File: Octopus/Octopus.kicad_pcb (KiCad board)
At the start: 2 copper layers, 205.8 x 111.7 mm, 61 parts, among them J1 FM6725 MIDI IN, J10 RN112BPC, J11 Button panel, J12 FM6725 MIDI THRU, J2 9-12VDC IN, J3 RN112BPC, J4 RN112BPC, J5 RN112BPC, J6 RN112BPC, J7 RN112BPC, J8 RN112BPC, J9 RN112BPC, K1 G5V-1, K10 G5V-1, K11 G5V-1, K12 G5V-1, K13 G5V-1, K14 G5V-1, K15 G5V-1, K16 G5V-1, K2 G5V-1, K3 G5V-1, K4 G5V-1, K5 G5V-1, K6 G5V-1, K7 G5V-1, K8 G5V-1, K9 G5V-1, U1 Teensy4.1, U2 6N138, U3 ULN2803A, U4 R-78E5.0-1.0, U5 ULN2803A, U6 74HCT14

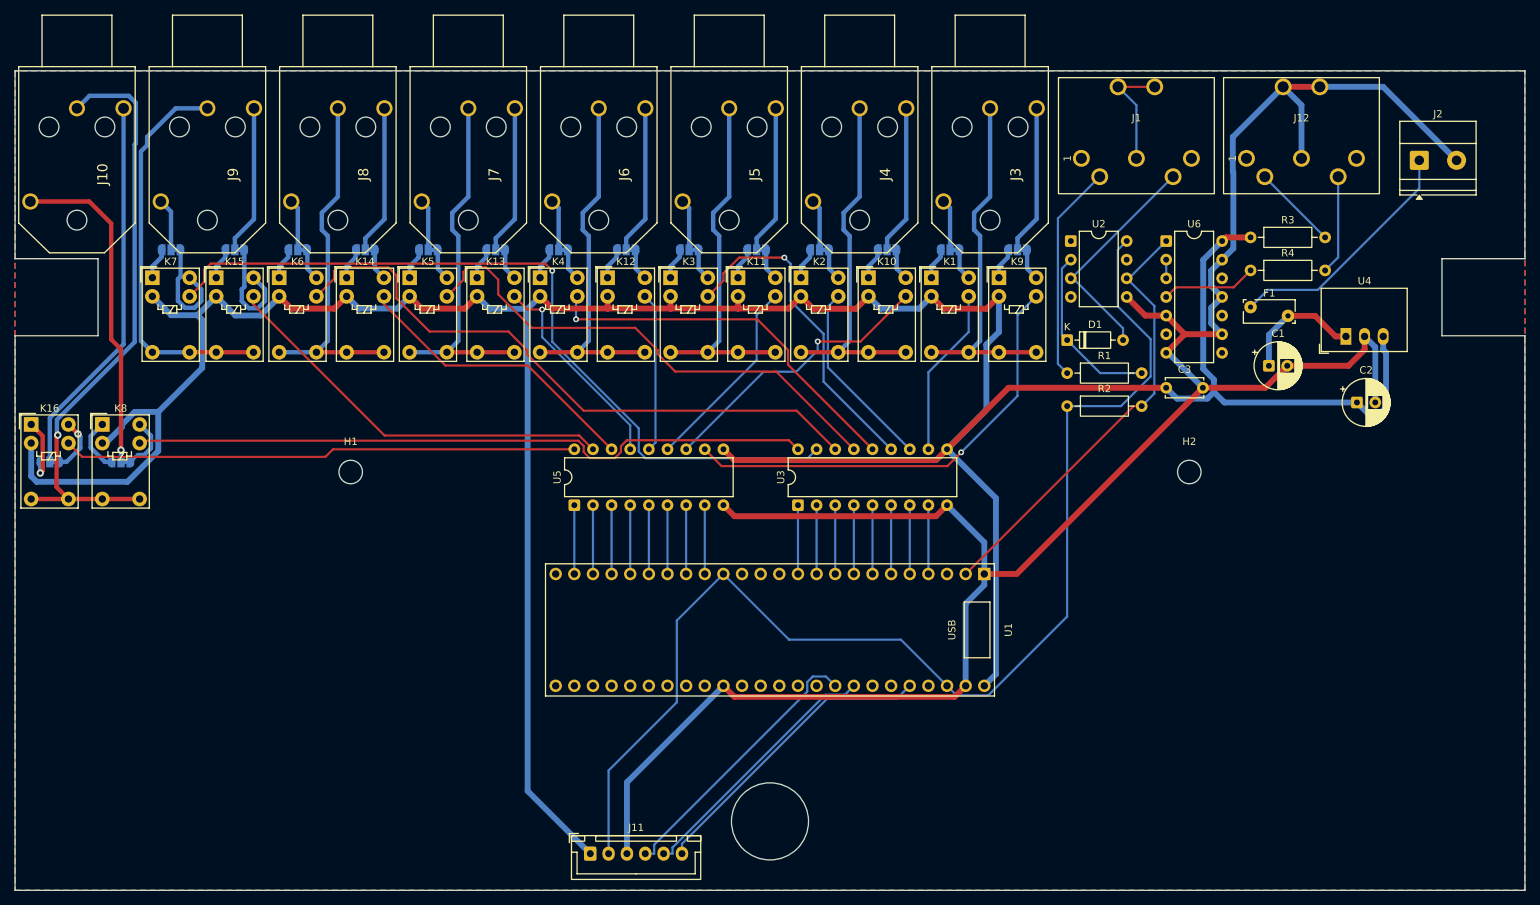
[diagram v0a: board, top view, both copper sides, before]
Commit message: Added standard power supply
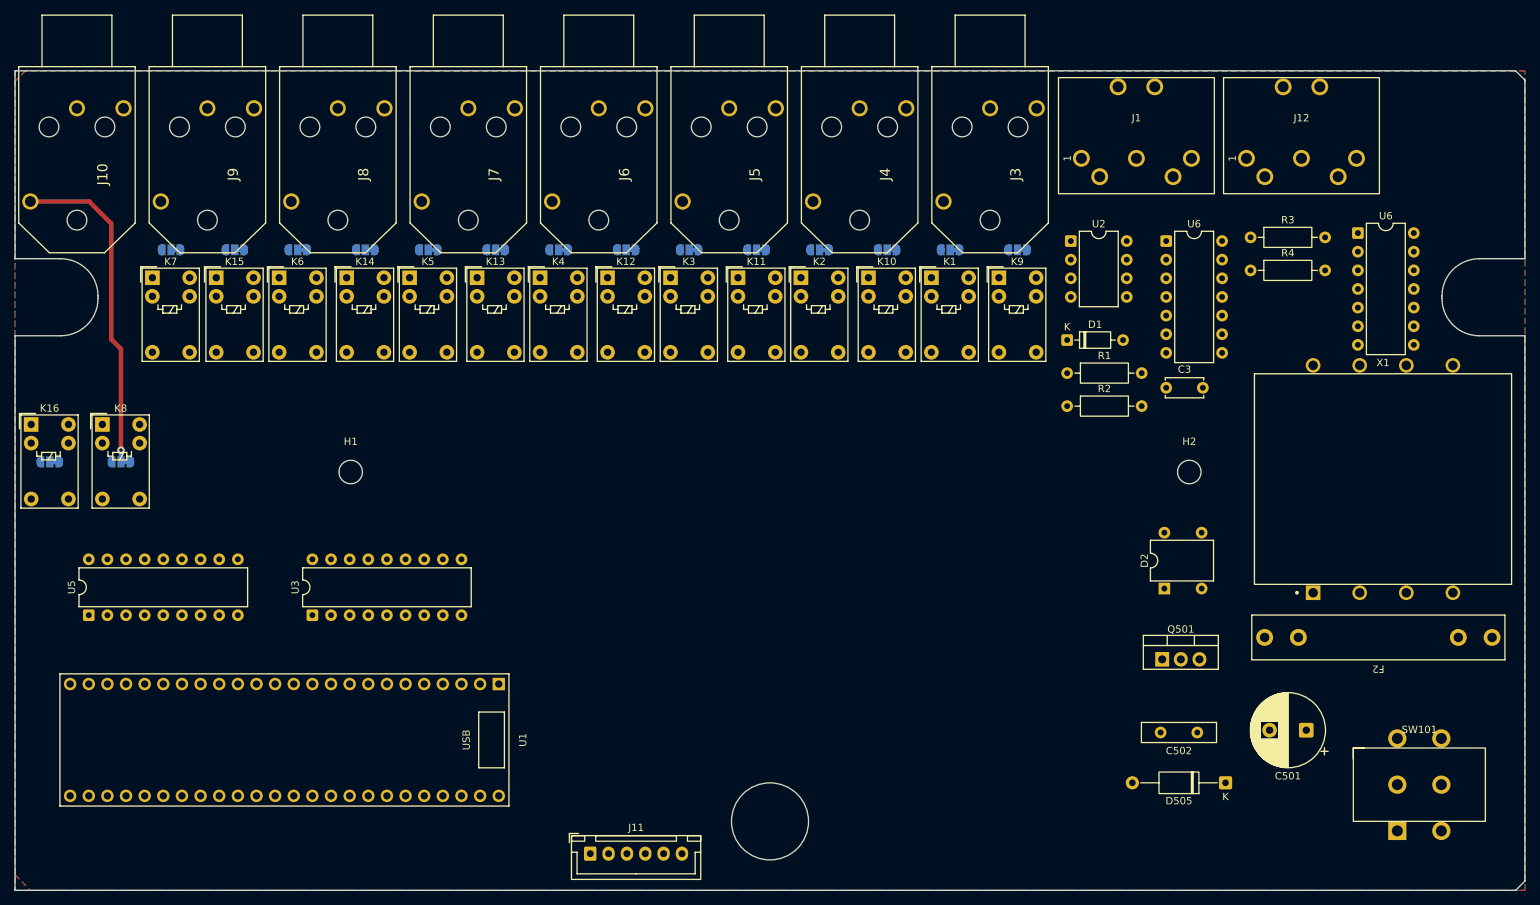
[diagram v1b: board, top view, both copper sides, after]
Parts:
- removed C1: 10uF 25V, Capacitor_THT:CP_Radial_D6.3mm_P2.50mm
- removed C2: 22uF 16V, Capacitor_THT:CP_Radial_D6.3mm_P2.50mm
- removed F1: MF-RHT070 0.7A, Fuse:Fuse_Bourns_MF-RHT070
- removed J2: 9-12VDC IN, TerminalBlock_Phoenix:TerminalBlock_Phoenix_MKDS-1,5-2-5.08_1x02_P5.08mm_Horizontal
- removed U4: R-78E5.0-1.0, Converter_DCDC:Converter_DCDC_RECOM_R-78E-0.5_THT
- added C501: 1000u, Capacitor_THT:CP_Radial_D10.0mm_P5.00mm, F.Cu at (223.1, 125.7)
- added C502: 100n, Capacitor_THT:C_Disc_D10.0mm_W2.5mm_P5.00mm, F.Cu at (208.2, 126.0)
- added D2: DF005M, Diode_THT:Diode_Bridge_DIP-4_W7.62mm_P5.08mm, F.Cu at (203.8, 106.4)
- added D505: 1N4001, Diode_THT:D_A-405_P12.70mm_Horizontal, F.Cu at (212.1, 132.8)
- added F2: Fuse, Fuse:Fuseholder_Littelfuse_100_series_5x30mm, F.Cu at (248.4, 113.0)
- added Q501: L7805, Package_TO_SOT_THT:TO-220-3_Vertical, F.Cu at (203.5, 116.0)
- added SW101: NE1838EE, Rockman:NE18_2U_EE_P_6AMP, F.Cu at (238.5, 133.1)
- added U6: 74HCT14, Package_DIP:DIP-14_W7.62mm, F.Cu at (230.1, 57.9)
- added X1: PSS-332, Rockman:Transformer_Hammond_164D_1.1VA, F.Cu at (224.0, 106.9)
- moved U1 67.9 mm to (83.8, 127.0)
- moved U3 67.9 mm to (87.6, 110.0)
- moved U5 67.9 mm to (57.1, 110.0)
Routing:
- net +5V: track 461.4 -> 0.00 mm
- net GND: track 302.0 -> 0.00 mm
- net +3V3: track 165.3 -> 0.00 mm
- net /DRV7: track 107.2 -> 0.00 mm, vias 1 -> 0
- net /DRV8: track 93.3 -> 0.00 mm
- net /DRV6: track 85.4 -> 0.00 mm
- net /JACK8_SLV: track 83.1 -> 0.00 mm, vias 1 -> 0
- net /DRV16: track 70.2 -> 0.00 mm
- net /DRV5: track 69.5 -> 0.00 mm
- net /DRV9: track 62.2 -> 0.00 mm, vias 1 -> 0
- net /MIDI_RX: track 60.6 -> 0.00 mm
- net /DRV15: track 55.5 -> 0.00 mm
- net /JACK7_SLV: track 54.0 -> 0.00 mm
- net /CH16_OUT: track 52.4 -> 0.00 mm
- net /DRV4: track 52.1 -> 0.00 mm, vias 1 -> 0
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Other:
- outline, holes or cut-outs redrawn
